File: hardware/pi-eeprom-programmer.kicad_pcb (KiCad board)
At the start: 2 copper layers, 70 x 56 mm, 3 parts, among them J1 Raspberry Pi GPIO Connector, J2 Conn_01x03, U1 ZIF Socket

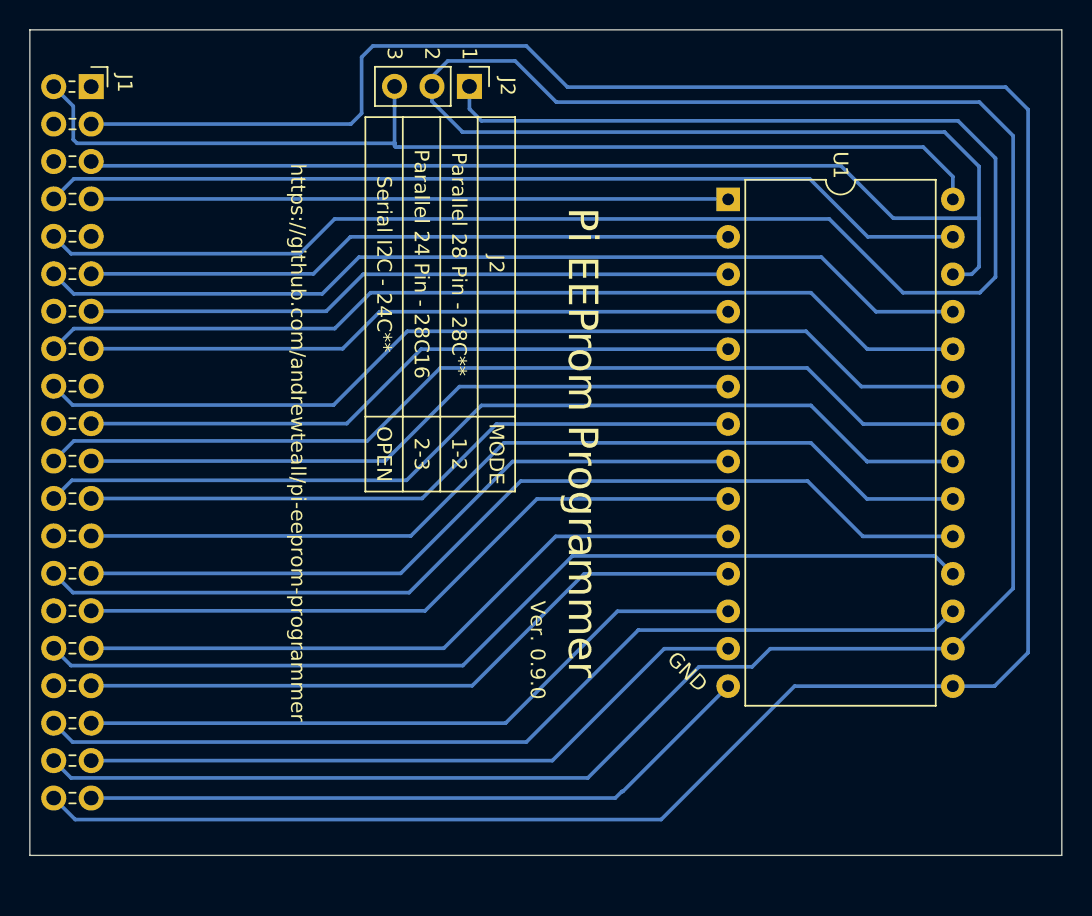
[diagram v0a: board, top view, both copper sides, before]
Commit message: Updated board to reuse GPIO 2 & 3 for Chardev switch
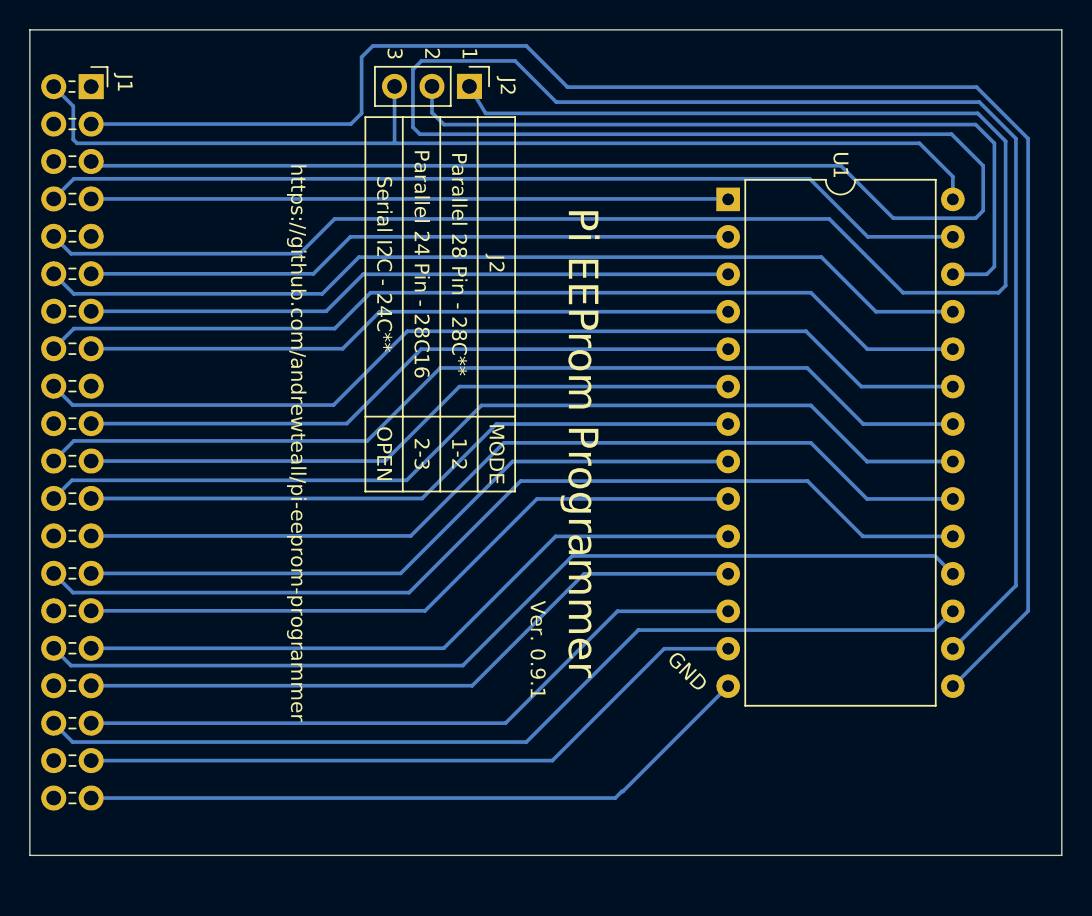
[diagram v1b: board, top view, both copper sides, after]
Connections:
- J1 pad 3: #21 -> SDA
- J1 pad 38: #20 -> unconnected-(J1-Pad38)
- J1 pad 40: #21 -> unconnected-(J1-Pad40)
- J1 pad 5: #20 -> SCL
- J2 pad 2: #20 -> SW_SEL
- U1 pad 15: #21 -> SDA
- U1 pad 16: #20 -> SCL
- U1 pad 26: #20 -> SW_SEL
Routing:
- net #20: track 254.8 -> 0.00 mm
- net SCL: track 0.00 -> 188.7 mm
- net #21: track 178.0 -> 0.00 mm
- net SDA: track 0.00 -> 109.8 mm
- net SW_SEL: track 0.00 -> 52.2 mm
- net RXD: track 114.5 -> 116.3 mm
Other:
- board text added: "Ver. 0.9.1"
- board text removed: "Ver. 0.9.0"

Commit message: Updated PCB to include spot for Serial EEPROM and updated README to reflect it
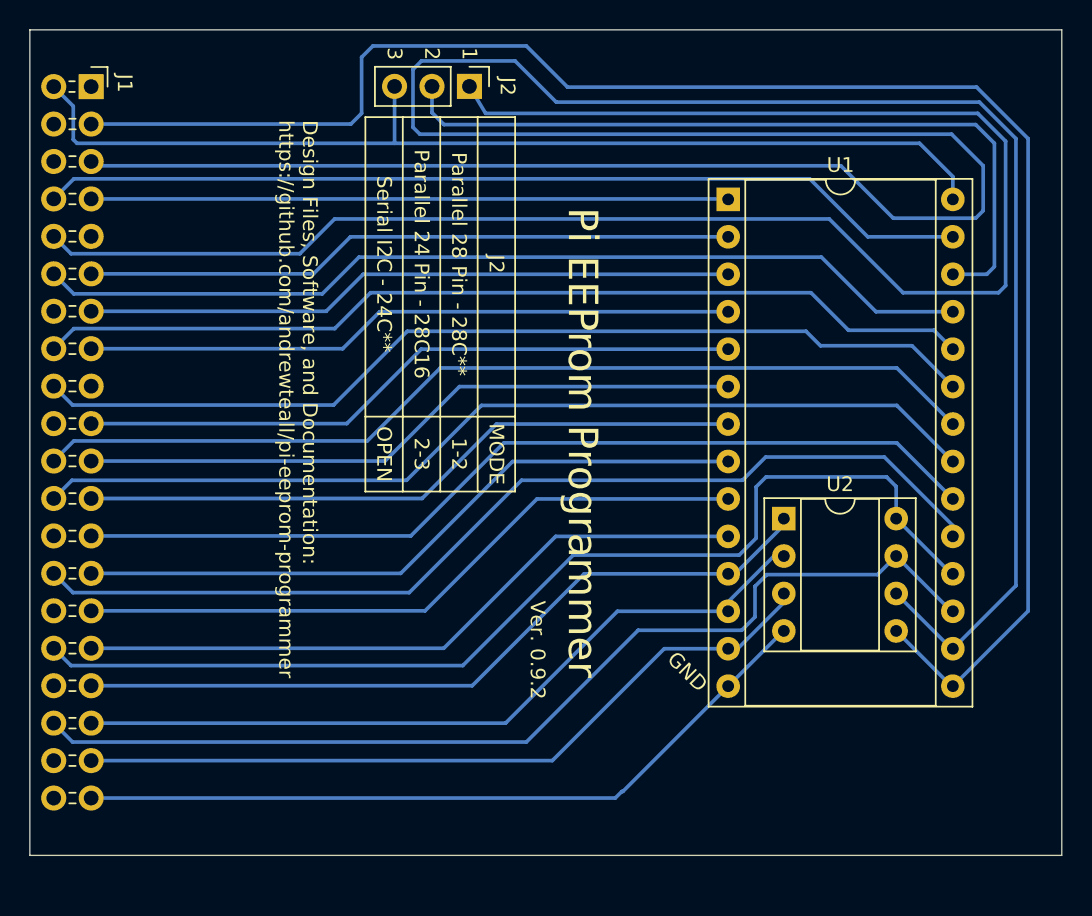
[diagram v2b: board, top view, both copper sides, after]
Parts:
- added U2: 24C01-24C1024, Package_DIP:DIP-8_W7.62mm_Socket, F.Cu at (183.6, 74.2)
- U1: footprint Package_DIP:DIP-28_W15.24mm -> Package_DIP:DIP-28_W15.24mm_Socket
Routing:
- net #12: track 65.1 -> 72.8 mm
- net #19: track 46.4 -> 52.1 mm
- net #26: track 46.4 -> 52.0 mm
- net #13: track 46.4 -> 51.9 mm
- net SDA: track 109.8 -> 115.2 mm
- net SCL: track 188.7 -> 194.1 mm
- net GND: track 46.4 -> 51.7 mm
- net #16: track 65.2 -> 69.5 mm
- net EEC: track 66.2 -> 68.0 mm
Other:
- board text added: "Design Files, Software, and Documentation: https://github.com/andrewteall/pi-eeprom-programmer"
- board text added: "Ver. 0.9.2"
- board text removed: "Ver. 0.9.1"
- board text removed: "https://github.com/andrewteall/pi-eeprom-programmer"
